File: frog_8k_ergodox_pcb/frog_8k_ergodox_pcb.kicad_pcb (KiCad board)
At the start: 2 copper layers, 8.7 x 17.3 mm, 214 parts, among them J1 USB_C_Receptacle_USB2.0_14P, J10 Conn_01x01_Pin, J2 Conn_01x04_Pin, J3 Conn_01x01_Pin, J4 Conn_01x01_Pin, J5 Conn_01x01_Pin, J6 Conn_01x01_Pin, J7 Conn_01x01_Pin, J8 Conn_01x01_Pin, J9 Conn_01x01_Pin, SW1 SW_DPST_x2, SW2 SW_DPST_x2, U2 STM32F072CBTx, U3 TLV74318PDBVR, U4 XC6206PxxxMR, U5 SRV05-4

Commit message: Rotated middle keys.
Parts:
- moved C1 142.2 mm to (353.3, 189.4)
- moved C4 142.2 mm to (353.3, 198.4)
- moved J2 142.2 mm to (348.8, 207.5)
- moved J3 142.2 mm to (324.8, 189.7)
- moved J4 142.2 mm to (324.8, 193.2)
- moved R1 142.2 mm to (320.6, 189.4)
- moved R3 142.2 mm to (320.6, 195.3)
- moved R7 142.2 mm to (351.8, 212.3)
- moved SW2 142.2 mm to (346.6, 197.9)
- moved U2 142.2 mm to (338.7, 209.3)
- moved U3 142.2 mm to (339.8, 190.3)
- moved U4 142.2 mm to (339.8, 194.9)
- moved U5 142.2 mm to (339.8, 199.5)
- moved C10 142.2 mm to (316.8, 198.7)
- moved C11 142.2 mm to (316.8, 200.7)
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
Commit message: Updated USB-C Position, Added PCB Edge Cut
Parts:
- C1, C10, C11, C12, C2, C3, C4, C5, C6, C7, C8, C9, F1, J10, J2, J3, J4, J5, J6, J7, J8, J9, R1, R2, R3, R5, R6, R7, SW1, SW2, U2, U3, U4, U5: moved to B.Cu
- moved J1 116.8 mm to (323.7, 92.7), turned to 180 degrees
- moved J2 91.2 mm to (323.6, 119.8)
- moved J3 88.0 mm to (378.2, 119.8), turned to 180 degrees
- moved J4 88.0 mm to (378.2, 123.4), turned to 180 degrees
- moved F1 87.2 mm to (324.1, 128.8), turned to -90 degrees
- moved D42 86.5 mm to (264.1, 153.1)
- moved D68 86.5 mm to (264.1, 191.2)
- moved D71 86.5 mm to (335.5, 191.2)
- moved D84 86.5 mm to (264.1, 210.3)
- moved D86 86.5 mm to (335.5, 210.3)
- moved MX28 86.5 mm to (264.2, 129.1)
- moved MX29 86.5 mm to (283.2, 129.1)
- moved MX30 86.5 mm to (307.0, 129.1)
- moved MX54 86.5 mm to (264.2, 167.2)
- moved MX55 86.5 mm to (283.2, 167.2)
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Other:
- board size 8.7 x 17.3 mm -> 344.7 x 123.6 mm

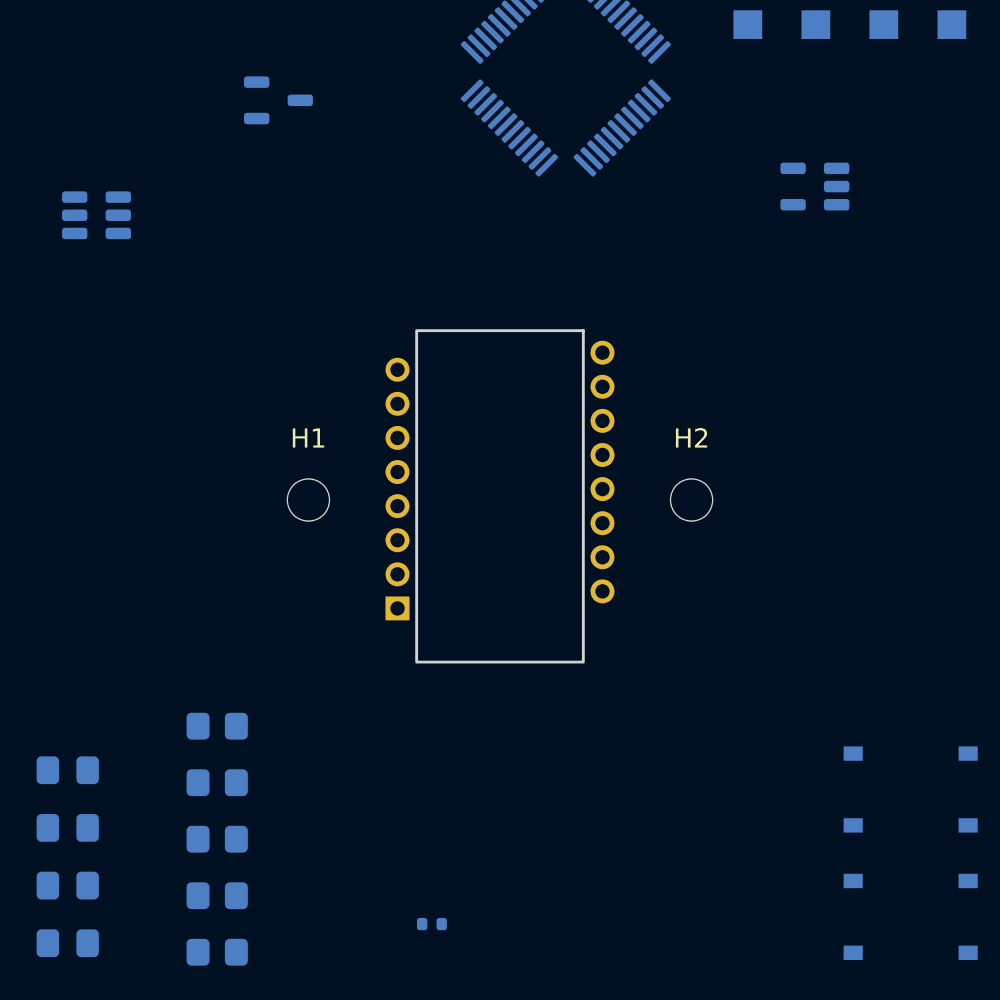
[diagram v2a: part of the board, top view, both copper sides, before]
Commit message: Updated TrackBall Housing Position & Mounting Hole Position.
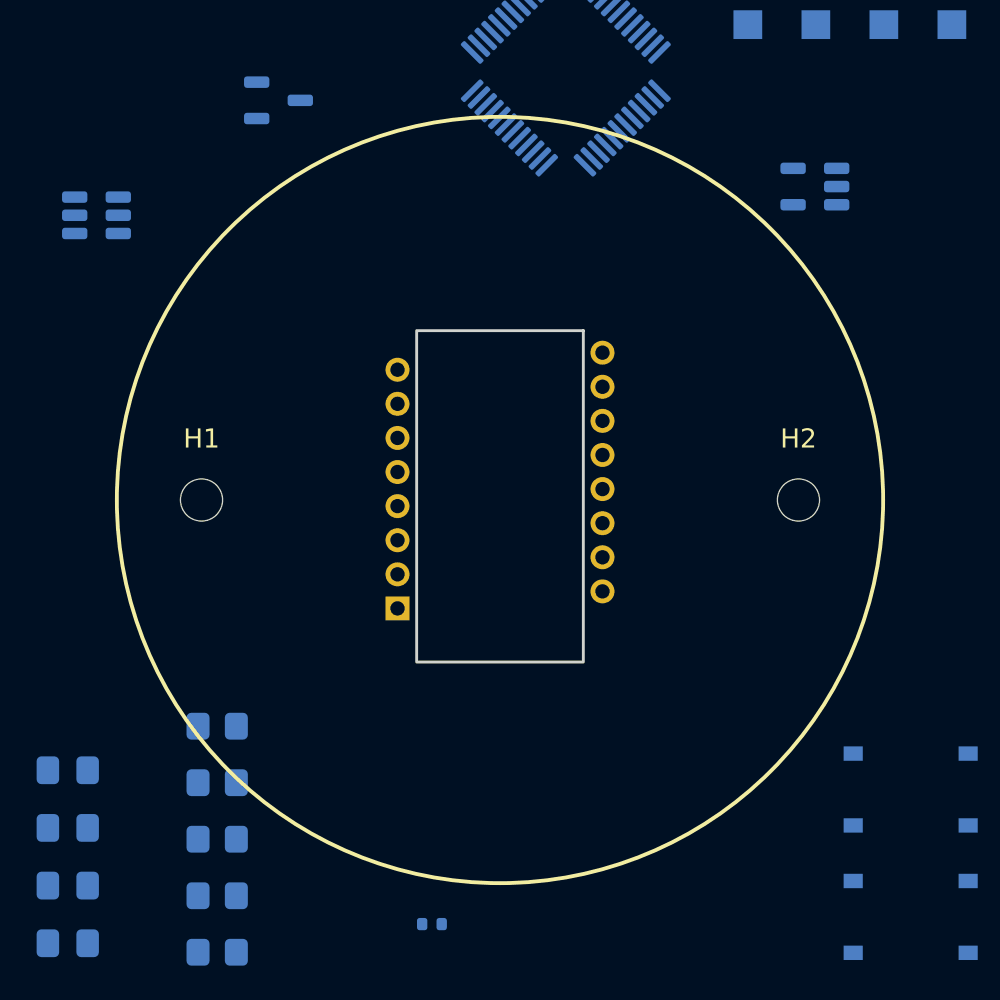
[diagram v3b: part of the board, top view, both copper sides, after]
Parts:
- moved H1 5.58 mm to (339.1, 148.2)
- moved H2 5.58 mm to (370.2, 148.2)
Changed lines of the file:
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@@
 	(footprint "MountingHole:MountingHole_2.2mm_M2"
 		(layer "F.Cu")
-		(at 344.6575 148.1975)
+		(at 339.077 148.1975)
 		(descr "Mounting Hole 2.2mm, no annular, M2")
 		(tags "mounting hole 2.2mm no annular m2")
@@
 		)
 		(property "Value" "MountingHole"
-			(at 0 3.2 0)
+			(at -0.077 3.8025 0)
 			(layer "F.Fab")
 			(effects
@@
 	(footprint "MountingHole:MountingHole_2.2mm_M2"
 		(layer "F.Cu")
-		(at 364.6575 148.1975)
+		(at 370.238 148.1975)
 		(descr "Mounting Hole 2.2mm, no annular, M2")
 		(tags "mounting hole 2.2mm no annular m2")
@@
 		(tags "SOT TO_SOT_SMD")
 		(property "Reference" "U4"
-			(at 0 2.4 360)
+			(at 0 2.4 0)
 			(layer "B.SilkS")
 			(effects
@@
 		)
 		(property "Value" "XC6206PxxxMR"
-			(at 0 -2.4 360)
+			(at 0 -2.4 0)
 			(layer "B.Fab")
 			(effects
@@
 		)
 		(fp_text user "${REFERENCE}"
-			(at 0 0 360)
+			(at 0 0 0)
 			(layer "B.Fab")
 			(effects
@@
 		)
 	)
+	(gr_circle
+		(center 354.6575 148.1975)
+		(end 374.6575 148.1975)
+		(stroke
+			(width 0.2)
+			(type default)
+		)
+		(fill none)
+		(layer "F.SilkS")
+	)
 	(gr_line
 		(start 354.6575 186.2975)
@@
 	)
 	(gr_line
-		(start 367.095 148.1975)
-		(end 340.595 148.1975)
+		(start 370.238 148.1975)
+		(end 339.077 148.1975)
 		(stroke
 			(width 0.05)
@@
 	)
 	(group ""
+		(members "38d0d4af-8ade-4b63-bcf6-dd296fe3a21a" "3a183d43-f6a3-4863-802b-183d6d596fe1"
+			"9d981614-73e0-4a59-9069-e09fc043286f" "c9de146f-9eab-457f-ac89-f95bdfe547ae"
+			"dc612385-4556-4ffc-97e3-922699310971" "fc919ac7-a472-4184-8ae4-cbe374104312"
+		)
+	)
+	(group ""

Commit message: Fixed matirix, Reconnect U1 Symbol to Footprint, relocate diode position.
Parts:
- moved D57 13.8 mm to (174.5, 173.2)
- moved D38 13.8 mm to (182.5, 161.5)
- moved D37 13.6 mm to (174.5, 161.3), turned to 90 degrees
- moved D58 13.4 mm to (182.5, 173.0), turned to -90 degrees
- moved D81 5.98 mm to (212.9, 210.0), turned to 90 degrees
- moved D85 5.98 mm to (312.9, 210.0), turned to 90 degrees
- moved D87 5.98 mm to (360.6, 210.0), turned to 90 degrees
- moved D88 5.98 mm to (379.6, 210.0), turned to 90 degrees
- moved D10 5.98 mm to (260.6, 110.0), turned to 90 degrees
- moved D11 5.98 mm to (279.6, 110.0), turned to 90 degrees
- moved D15 5.98 mm to (360.6, 110.0), turned to 90 degrees
- moved D16 5.98 mm to (379.6, 110.0), turned to 90 degrees
- moved D25 5.98 mm to (212.9, 133.8), turned to 90 degrees
- moved D29 5.98 mm to (289.1, 133.8), turned to 90 degrees
- moved D30 5.98 mm to (312.9, 133.8), turned to 90 degrees
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- renumbered REF** to U1-PMW3360
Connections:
- MX51 pad 1: COL6 -> COL8
- MX52 pad 1: COL7 -> COL9
- MX53 pad 1: COL8 -> COL10
- MX54 pad 1: COL9 -> COL11
- MX55 pad 1: COL10 -> COL12
- MX56 pad 1: COL11 -> COL13
- MX57 pad 1: COL12 -> COL6
- MX58 pad 1: COL13 -> COL7
- U1-PMW3360 pad 10: (no net) -> SCLK_{GPIO-PMW3360}
- U1-PMW3360 pad 11: (no net) -> MOSI_{GPIO-PMW3360}
- U1-PMW3360 pad 12: (no net) -> MISO_{GPIO-PMW3360}
- U1-PMW3360 pad 13: (no net) -> CS_{GPIO-PMW3360}
- U1-PMW3360 pad 15: (no net) -> Net-(U1-LED_P)
- U1-PMW3360 pad 3: (no net) -> Net-(U1-VDDPIX)
- U1-PMW3360 pad 4: (no net) -> VDD_{1.8V~2.1V}
- U1-PMW3360 pad 5: (no net) -> V_{IO VDD~3.3V}
- U1-PMW3360 pad 7: (no net) -> Net-(U1-~{RESET})
- U1-PMW3360 pad 8: (no net) -> GND

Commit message: Updated PCB design.
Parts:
- F1: value Fuse_500mA -> 500mA; footprint Fuse:Fuse_1206_3216Metric_Pad1.42x1.75mm_HandSolder -> Fuse:Fuse_1206_3216Metric
- moved R6 72.4 mm to (325.0, 101.0), turned to -90 degrees
- moved R5 70.3 mm to (321.5, 101.0), turned to -90 degrees
- moved U3 36.1 mm to (352.0, 162.5), turned to 0 degrees
- moved R3 30.8 mm to (368.5, 154.5), turned to -90 degrees
- moved R2 30.7 mm to (350.0, 134.0), turned to 0 degrees
- moved R1 30.6 mm to (350.0, 131.2), turned to 0 degrees
- moved U5 28.4 mm to (323.0, 107.0), turned to 90 degrees
- moved F1 27.1 mm to (327.5, 102.0)
- moved C2 24.8 mm to (340.5, 142.0)
- moved C1 24.8 mm to (340.5, 139.0)
- moved U4 23.0 mm to (326.0, 112.0), turned to 180 degrees
- moved U2 20.9 mm to (337.5, 122.0), turned to 135 degrees
- moved C3 18.9 mm to (345.5, 155.0)
- moved C4 17.1 mm to (340.5, 156.5), turned to -90 degrees
- moved C10 16.9 mm to (325.5, 147.9)
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- renumbered U1-PMW3360 to U1
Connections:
- U1 pad 1: (no net) -> unconnected-(U1-NC-Pad1)
- U1 pad 14: (no net) -> unconnected-(U1-NC-Pad14)
- U1 pad 16: (no net) -> unconnected-(U1-NC-Pad16)
- U1 pad 2: (no net) -> unconnected-(U1-NC-Pad2)
- U1 pad 6: (no net) -> unconnected-(U1-NC-Pad6)
- U1 pad 9: (no net) -> unconnected-(U1-MOTION-Pad9)
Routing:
- net DP: track 0.00 -> 44.0 mm, vias 0 -> 1
- net DN: track 0.00 -> 40.5 mm, vias 0 -> 1
- net +3V3: track 0.00 -> 37.4 mm, vias 0 -> 2
- net +5V: track 0.00 -> 19.7 mm
- net VBUS: track 0.00 -> 11.8 mm, vias 0 -> 1
- net Net-(D30-A): track 0.00 -> 9.99 mm
- net Net-(D29-A): track 0.00 -> 9.99 mm
- net Net-(D14-A): track 0.00 -> 9.99 mm
- net Net-(D2-A): track 0.00 -> 9.99 mm
- net Net-(D1-A): track 0.00 -> 9.99 mm
- net Net-(D4-A): track 0.00 -> 9.99 mm
- net Net-(D3-A): track 0.00 -> 9.99 mm
- net Net-(D27-A): track 0.00 -> 9.99 mm
- net Net-(D12-A): track 0.00 -> 9.99 mm
- net Net-(D8-A): track 0.00 -> 9.99 mm
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
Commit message: Fixed USB Port 5V to 3.3V, Added Matrix Row/Col
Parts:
- H1: footprint MountingHole:MountingHole_2.2mm_M2 -> MountingHole:MountingHole_2.2mm_M2_ISO14580_Pad
- H2: footprint MountingHole:MountingHole_2.2mm_M2 -> MountingHole:MountingHole_2.2mm_M2_ISO7380_Pad
- moved C6 52.5 mm to (372.5, 116.5), turned to 90 degrees
- moved SW2 49.6 mm to (373.0, 122.5), turned to -90 degrees
- moved SW1 49.5 mm to (365.1, 122.5), turned to -90 degrees
- moved J9 48.2 mm to (320.9, 131.8)
- moved J3 48.2 mm to (331.6, 131.8)
- moved J5 48.2 mm to (328.1, 131.8)
- moved J7 48.2 mm to (324.5, 131.8)
- moved J10 47.9 mm to (320.9, 136.5)
- moved J4 47.9 mm to (331.6, 136.5)
- moved J6 47.9 mm to (328.1, 136.5)
- moved J8 47.9 mm to (324.5, 136.5)
- moved C9 34.7 mm to (348.0, 119.5), turned to 45 degrees
- moved C10 32.6 mm to (348.1, 124.3), turned to -45 degrees
- moved C8 31.5 mm to (339.0, 115.5), turned to 135 degrees
- moved C11 30.0 mm to (345.2, 127.2), turned to -45 degrees
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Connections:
- U5 pad 3: DP -> unconnected-(U5-IO2-Pad3)
- U5 pad 4: unconnected-(U5-IO3-Pad4) -> DN
- U5 pad 6: DN -> DP
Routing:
- net ROW0: track 0.00 -> 328.7 mm, vias 0 -> 2
- net ROW5: track 0.00 -> 324.3 mm
- net ROW4: track 0.00 -> 323.9 mm
- net ROW2: track 0.00 -> 265.8 mm
- net ROW3: track 0.00 -> 259.7 mm
- net ROW1: track 0.00 -> 257.2 mm
- net COL14: track 0.00 -> 186.9 mm
- net COL15: track 0.00 -> 149.8 mm
- net COL16: track 0.00 -> 113.1 mm
- net COL10: track 0.00 -> 109.2 mm
- net COL11: track 0.00 -> 106.6 mm
- net COL6: track 0.00 -> 106.5 mm
- net COL2: track 0.00 -> 105.9 mm
- net COL3: track 0.00 -> 105.7 mm
- net COL4: track 0.00 -> 105.6 mm
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
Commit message: Added plate file, Updated Matrix route, Additional Pin routes
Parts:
- moved J9 43.2 mm to (364.1, 131.0)
- moved J3 43.2 mm to (374.8, 131.0)
- moved J5 43.2 mm to (371.2, 131.0)
- moved J7 43.2 mm to (367.6, 131.0)
- moved C1 29.0 mm to (369.5, 139.0)
- moved C2 29.0 mm to (369.5, 142.0)
- moved R2 16.7 mm to (366.5, 136.5)
- moved D88 14.6 mm to (374.4, 196.4), turned to 0 degrees
- moved R1 13.7 mm to (342.2, 142.5)
- moved D79 10.9 mm to (177.0, 199.3), turned to -90 degrees
- moved D84 10.9 mm to (272.2, 199.3), turned to -90 degrees
- moved D85 10.9 mm to (315.1, 199.3), turned to -90 degrees
- moved D76 10.9 mm to (119.8, 199.3), turned to -90 degrees
- moved D74 10.9 mm to (57.9, 199.3), turned to -90 degrees
- moved D75 10.9 mm to (100.8, 199.3), turned to -90 degrees
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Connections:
- U2 pad 11: ADD7 -> COL15
- U2 pad 12: ADD6 -> ROW5
- U2 pad 13: ADD5 -> COL12
- U2 pad 25: COL12 -> ADD7
- U2 pad 26: COL13 -> ADD6
- U2 pad 27: COL14 -> ADD5
- U2 pad 28: COL15 -> ADD4
- U2 pad 29: ADD4 -> ADD3
- U2 pad 30: ADD3 -> ADD2
- U2 pad 31: ADD2 -> ADD1
- U2 pad 34: ADD1 -> ADD0
- U2 pad 37: ADD0 -> COL14
- U2 pad 38: ROW5 -> COL13
- U2 pad 39: COL3 -> unconnected-(U2-PB3-Pad39)
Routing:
- net ADD6: track 0.00 -> 72.0 mm, vias 0 -> 2
- net ADD4: track 0.00 -> 69.9 mm, vias 0 -> 2
- net ADD2: track 0.00 -> 68.5 mm, vias 0 -> 2
- net ADD0: track 0.00 -> 60.6 mm, vias 0 -> 2
- net MISO_{GPIO-PMW3360}: track 0.00 -> 47.1 mm, vias 0 -> 2
- net CS_{GPIO-PMW3360}: track 0.00 -> 40.0 mm, vias 0 -> 2
- net MOSI_{GPIO-PMW3360}: track 0.00 -> 40.0 mm, vias 0 -> 2
- net SCLK_{GPIO-PMW3360}: track 0.00 -> 34.2 mm, vias 0 -> 2
- net ADD7: track 0.00 -> 30.9 mm, vias 0 -> 2
- net ADD5: track 0.00 -> 29.7 mm, vias 0 -> 2
- net ADD3: track 0.00 -> 28.1 mm, vias 0 -> 2
- net ADD1: track 0.00 -> 27.1 mm, vias 0 -> 2
- net RST-1: track 0.00 -> 20.7 mm
- net +3V3: track 46.3 -> 64.8 mm
- net BOOT-1: track 0.00 -> 12.9 mm
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
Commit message: updated footprints...
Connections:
- U2 pad 39: unconnected-(U2-PB3-Pad39) -> COL3
